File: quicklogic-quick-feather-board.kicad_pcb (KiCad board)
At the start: 6 copper layers, 50.8 x 22.9 mm, 118 parts, among them IC1 EOS-S3, J1 825437-4, J2 1x12_pinhead, J3 1x16_pinhead, J4 S2B-PH-SM4-TB_LF__SN_, J5 0473460001, J6 FTSH-105-01-L-DV-K, Q1 RV1C002UN, Q2 RV1C001ZP, Q3 RV1C002UN, Q4 RV1C002UN, Q5 RV1C002UN, U1 TPS62821DLCR, U2 MCP73831T-2ACI_OT, U3 GD25Q16CWIGR, U4 DPS310, U5 MC3635, X1 ECS-_327-12_5-34B-TR

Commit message: Updated 3D vis
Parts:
- moved J1 4.09 mm to (163.0, 100.9)
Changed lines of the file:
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@@
     (34 B.Paste user hide)
     (35 F.Paste user hide)
-    (36 B.SilkS user hide)
+    (36 B.SilkS user)
     (37 F.SilkS user)
     (38 B.Mask user hide)
@@
   )
   (module quicklogic-quick-feather-board-footprints:TE_825437-4 (layer Bottom)
-    (at 162.95 105.0036 270)
-    (fp_text reference J1 (at -6.46 1.8 180) (layer B.SilkS)
+    (at 162.96 100.91 270)
+    (fp_text reference J1 (at -2.48 1.99 180) (layer B.SilkS)
       (effects (font (size 0.7 0.7) (thickness 0.15)) (justify mirror))
     )
@@
     (pad 1 smd rect (at -1 0) (size 1 3.5) (layers Top F.Paste F.Mask)
       (net 1 GND))
+    (model ${KIPRJMOD}/lib/3d-models/S2B-PH-SM4-TB.step
+      (offset (xyz 0 7 0))
+      (scale (xyz 1 1 1))
+      (rotate (xyz 0 0 -180))
+    )
   )
   (module quicklogic-quick-feather-board-footprints:PinHeader_2x5_P1.27_SMD (layer Top)
@@
     (tags resistor)
     (attr smd)
-    (fp_text reference C18 (at 0 1.17 270) (layer B.SilkS)
+    (fp_text reference C18 (at -0.12 -0.97 270) (layer B.SilkS)
       (effects (font (size 0.7 0.7) (thickness 0.15)) (justify mirror))
     )
@@
     (tags resistor)
     (attr smd)
-    (fp_text reference R29 (at -2.1 -0.2) (layer F.SilkS)
+    (fp_text reference R29 (at -2.05 -0.05) (layer F.SilkS)
       (effects (font (size 0.7 0.7) (thickness 0.15)))
     )
@@
     (tags resistor)
     (attr smd)
-    (fp_text reference R27 (at -2 0.15) (layer F.SilkS)
-      (effects (font (size 0.7 0.7) (thickness 0.15)))
-    )
+    (fp_text reference R27 (at -2.06 0.34) (layer F.SilkS)
+      (effects (font (size 0.7 0.7) (thickness 0.15)))
+    )

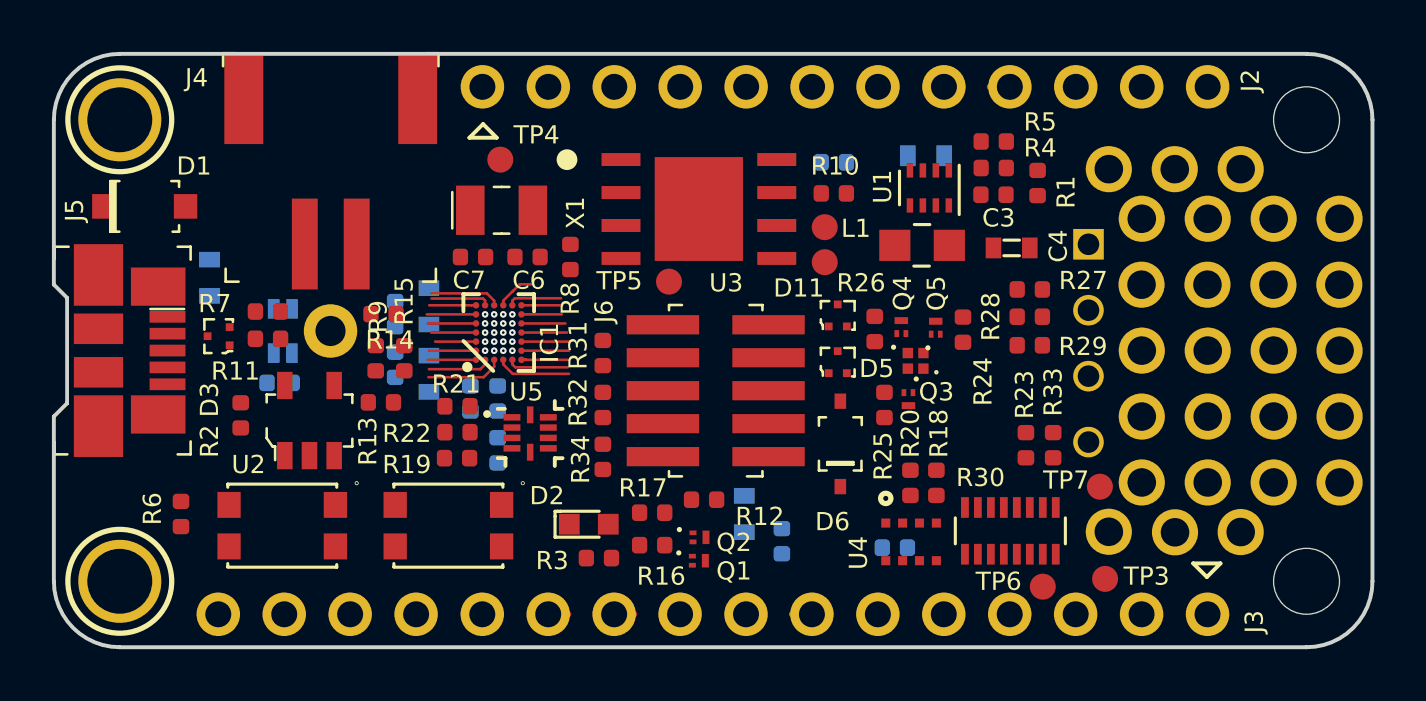
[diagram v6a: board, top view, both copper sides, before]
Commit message: Updated component placement, added 3D models for pin headers
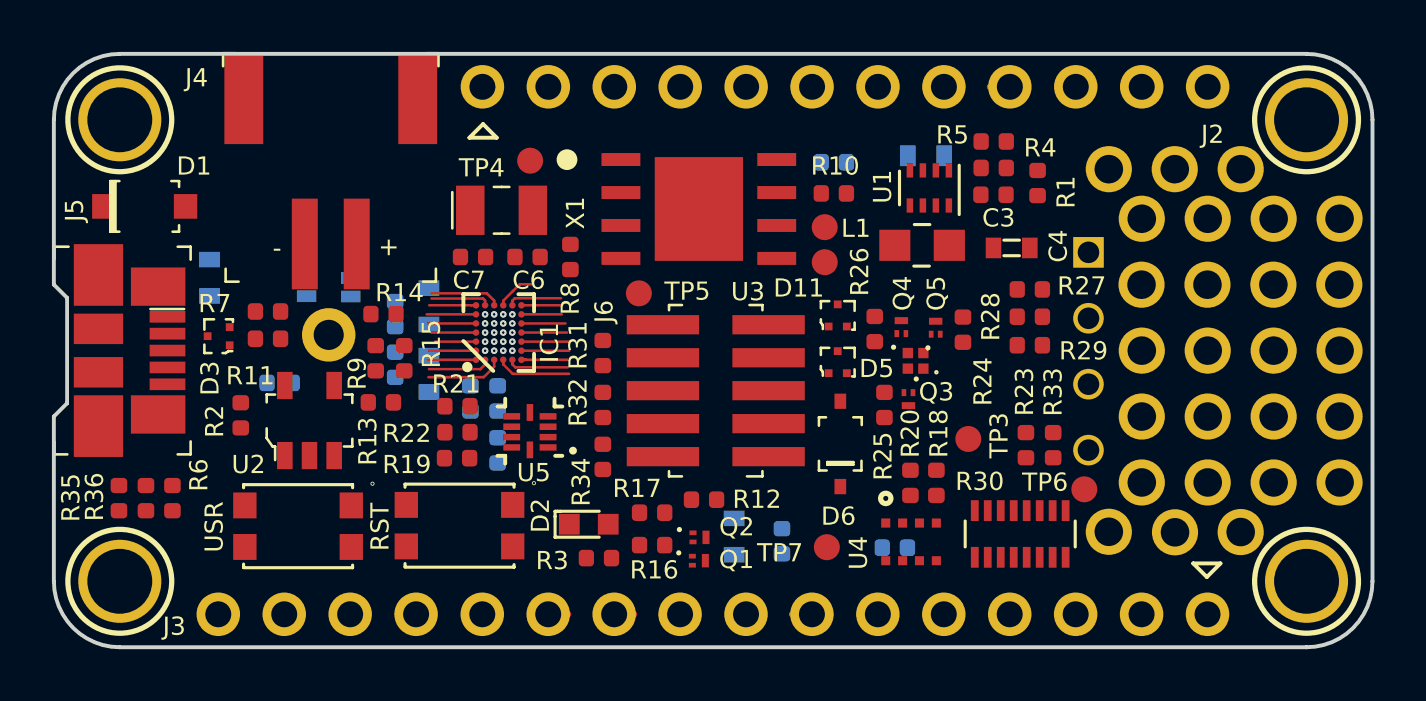
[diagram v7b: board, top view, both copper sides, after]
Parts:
- removed @HOLE0 (x2): , 
- added R35: R_0R_0402, quicklogic-quick-feather-board-footprints:0402-res, F.Cu at (125.6, 110.7)
- added R36: R_10k_0402, quicklogic-quick-feather-board-footprints:0402-res, F.Cu at (126.7, 110.7)
- added U$31: MOUNTINGHOLE2.5, MOUNTINGHOLE_2.5_PLATED, F.Cu at (171.4, 113.9)
- added U$31: MOUNTINGHOLE2.5, MOUNTINGHOLE_2.5_PLATED, F.Cu at (171.4, 96.1)
- moved TP7 10.8 mm to (152.9, 112.6)
- moved TP3 7.54 mm to (158.3, 108.5)
- moved J1 4.12 mm to (163.0, 105.0)
- moved TP6 4.08 mm to (162.8, 110.4)
- moved TP5 1.24 mm to (145.6, 102.8)
- moved TP4 1.15 mm to (141.4, 97.7)
- moved C2 0.95 mm to (149.3, 112.2)
- moved R6 0.69 mm to (127.7, 110.7)
- moved S2 0.61 mm to (132.5, 111.8)
- moved U5 0.52 mm to (141.2, 108.1), turned to 180 degrees
- moved S1 0.43 mm to (138.7, 111.8)
- moved R30 0.40 mm to (160.3, 112.1)
- moved MIC1 0.15 mm to (133.7, 104.4), turned to 0 degrees
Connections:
- J5 pad 4: GND -> /USB_ID
- R30 pad 10: Net-(J3-Pad3) -> /HEADER_RX
- R30 pad 11: Net-(J3-Pad4) -> /HEADER_MISO
- R30 pad 12: Net-(J3-Pad5) -> /HEADER_MOSI
- R30 pad 13: Net-(J3-Pad6) -> /HEADER_SCK
- R30 pad 14: Net-(J3-Pad7) -> /HEADER_A5
- R30 pad 3: /HEADER_A5 -> Net-(J3-Pad7)
- R30 pad 4: /HEADER_SCK -> Net-(J3-Pad6)
- R30 pad 5: /HEADER_MOSI -> Net-(J3-Pad5)
- R30 pad 6: /HEADER_MISO -> Net-(J3-Pad4)
- R30 pad 7: /HEADER_RX -> Net-(J3-Pad3)
- R30 pad 8: /HEADER_TX -> Net-(J3-Pad2)
- R30 pad 9: Net-(J3-Pad2) -> /HEADER_TX
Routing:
- net /SPI_MST_CLK: vias 3 -> 2
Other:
- board text added: "+"
- board text added: "-"
- board text added: "RST"
- board text added: "USR"

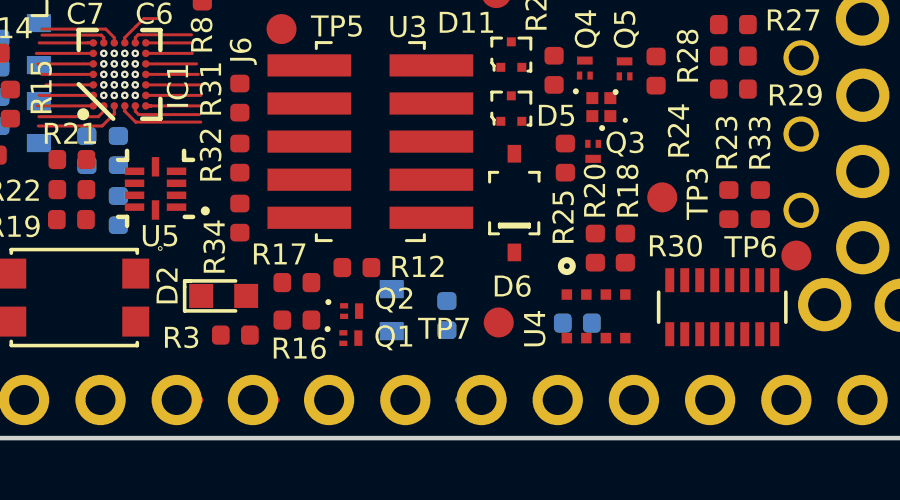
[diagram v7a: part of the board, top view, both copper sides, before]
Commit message: Added some MPNs to libraries and updated them on schematic, updated BOM and schematic PDF
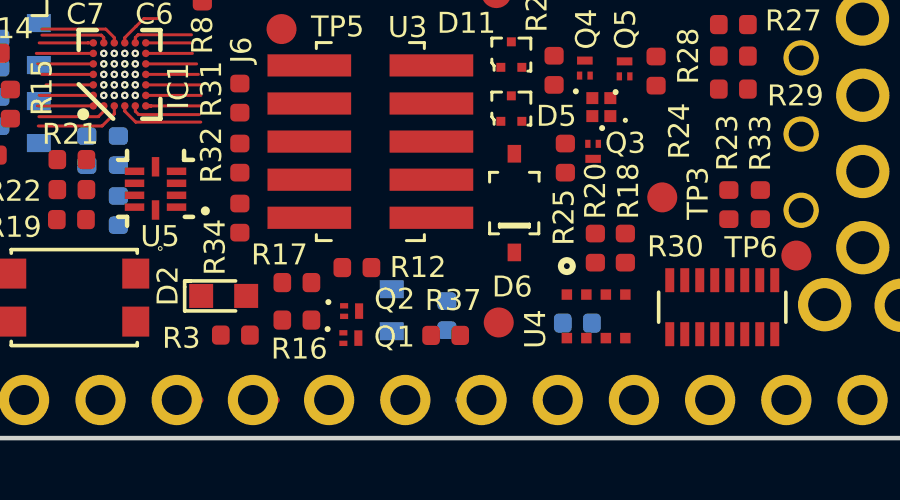
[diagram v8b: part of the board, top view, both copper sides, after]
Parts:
- added R37: R_10k_0402, quicklogic-quick-feather-board-footprints:0402-res, F.Cu at (151.1, 113.0)
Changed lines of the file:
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@@
     (tracks 112)
     (zones 0)
-    (modules 120)
+    (modules 121)
     (nets 94)
   )
@@
   )
   (module quicklogic-quick-feather-board-footprints:0402-res (layer Top)
+    (at 151.11 113.01)
+    (descr "Resistor SMD 0402 (1005 Metric), square (rectangular) end terminal, IPC_7351 nominal, (Body size source: http://www.tortai-tech.com/upload/download/2011102023233369053.pdf), generated with kicad-footprint-generator")
+    (tags resistor)
+    (attr smd)
+    (fp_text reference R37 (at 0.25 -1.17) (layer F.SilkS)
+      (effects (font (size 0.7 0.7) (thickness 0.15)))
+    )
+    (fp_text value R_10k_0402 (at 0 1.17) (layer F.Fab)
+      (effects (font (size 1 1) (thickness 0.15)))
+    )
+    (fp_text user %R (at 0 0) (layer F.Fab)
+      (effects (font (size 0.25 0.25) (thickness 0.04)))
+    )
+    (fp_line (start 0.93 0.47) (end -0.93 0.47) (layer F.CrtYd) (width 0.05))
+    (fp_line (start 0.93 -0.47) (end 0.93 0.47) (layer F.CrtYd) (width 0.05))
+    (fp_line (start -0.93 -0.47) (end 0.93 -0.47) (layer F.CrtYd) (width 0.05))
+    (fp_line (start -0.93 0.47) (end -0.93 -0.47) (layer F.CrtYd) (width 0.05))
+    (fp_line (start 0.5 0.25) (end -0.5 0.25) (layer F.Fab) (width 0.1))
+    (fp_line (start 0.5 -0.25) (end 0.5 0.25) (layer F.Fab) (width 0.1))
+    (fp_line (start -0.5 -0.25) (end 0.5 -0.25) (layer F.Fab) (width 0.1))
+    (fp_line (start -0.5 0.25) (end -0.5 -0.25) (layer F.Fab) (width 0.1))
+    (pad 2 smd roundrect (at 0.485 0) (size 0.59 0.64) (layers Top F.Paste F.Mask) (roundrect_rratio 0.25)
+      (net 1 GND))
+    (pad 1 smd roundrect (at -0.485 0) (size 0.59 0.64) (layers Top F.Paste F.Mask) (roundrect_rratio 0.25)
+      (net 31 /ADC0_EN))
+    (model ${KIPRJMOD}/lib/3d-models/0402-res.step
+      (offset (xyz 0 0 -0.01))
+      (scale (xyz 1 1 1))
+      (rotate (xyz 0 0 0))
+    )
+  )
+  (module quicklogic-quick-feather-board-footprints:0402-res (layer Top)
     (at 126.65 110.69 270)
     (descr "Resistor SMD 0402 (1005 Metric), square (rectangular) end terminal, IPC_7351 nominal, (Body size source: http://www.tortai-tech.com/upload/download/2011102023233369053.pdf), generated with kicad-footprint-generator")
@@
   (module quicklogic-quick-feather-board-footprints:Testpoint_smd_1mm (layer Top)
     (at 152.88 112.63)
-    (fp_text reference TP7 (at -1.8 0.17) (layer F.SilkS)
-      (effects (font (size 0.7 0.7) (thickness 0.15)))
-    )
+    (fp_text reference TP7 (at -0.59 0.96) (layer F.SilkS) hide
+      (effects (font (size 0.7 0.7) (thickness 0.15)))
+    )
